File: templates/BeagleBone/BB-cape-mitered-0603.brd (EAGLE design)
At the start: 86.4 x 54.6 mm, 14 parts, among them IC8 EEPROM-I2CSMD

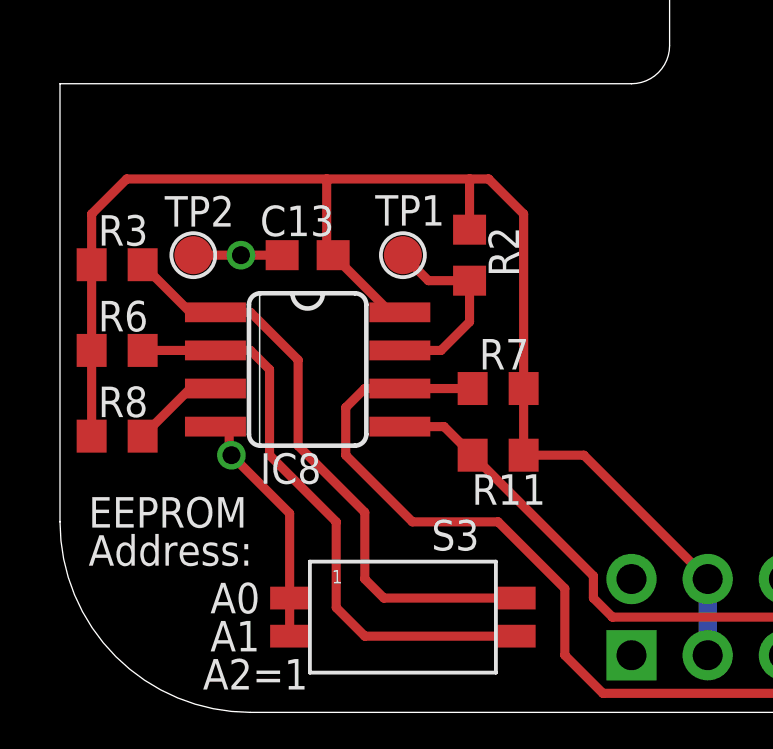
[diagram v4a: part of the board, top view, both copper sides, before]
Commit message: renumbered components on templates
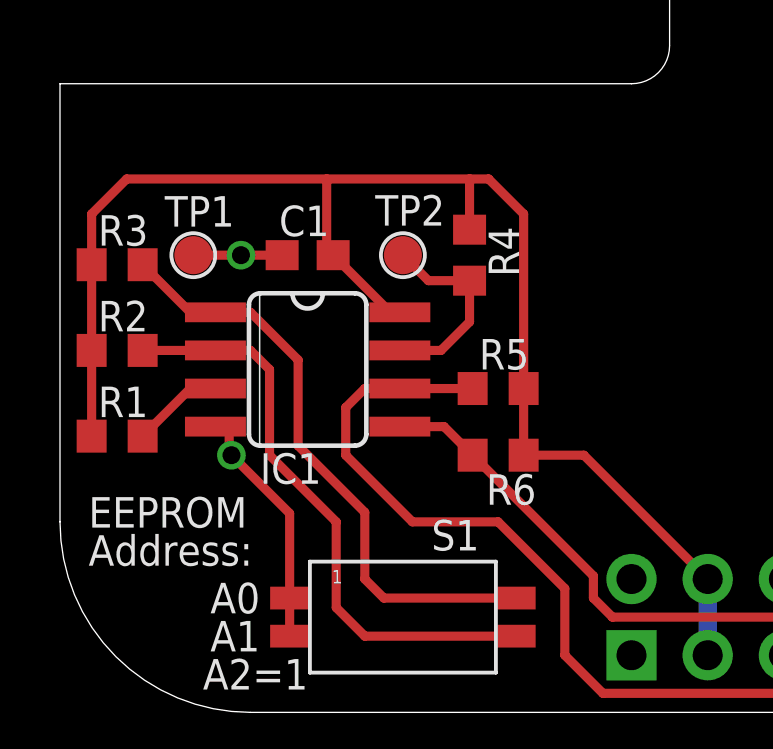
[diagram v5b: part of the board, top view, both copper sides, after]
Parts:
- removed R11: 5.6k, rcl:R0603
- added R4: 5.6k, rcl:R0603
- moved R6 13.2 mm to (14.6, 8.57), turned to 0 degrees
- moved R2 12.2 mm to (1.91, 12.1), turned to 180 degrees
- moved TP1 6.98 mm to (4.45, 15.2)
- moved TP2 6.98 mm to (11.4, 15.2)
- renumbered C13 to C1, IC8 to IC1, R7 to R5, R8 to R1, S3 to S1
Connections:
- net 3.3V: now also R4.2; no longer R11.2
- net GND: now also TP1.P$1; no longer TP2.P$1
- net I2C2_SDA: now also R6.1; no longer R11.1
- net N$14: now also R2.1; no longer R6.1
- net WP: now also R4.1, TP2.P$1; no longer R2.1, TP1.P$1
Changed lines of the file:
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@@
 <layer number="220" name="220bmp" color="21" fill="1" visible="no" active="no"/>
 <layer number="221" name="221bmp" color="22" fill="1" visible="no" active="no"/>
-<layer number="222" name="222bmp" color="23" fill="1" visible="no" active="no"/>
 <layer number="223" name="223bmp" color="24" fill="1" visible="no" active="no"/>
 <layer number="224" name="224bmp" color="25" fill="1" visible="no" active="no"/>
@@
 </autorouter>
 <elements>
-<element name="IC8" library="logic-supply" package="SO08" value="EEPROM-I2CSMD" x="8.255" y="11.43" smashed="yes" rot="R270">
+<element name="IC1" library="logic-supply" package="SO08" value="EEPROM-I2CSMD" x="8.255" y="11.43" smashed="yes" rot="R270">
 <attribute name="VALUE" x="7.62" y="12.7" size="0.4064" layer="27" rot="R270"/>
 <attribute name="NAME" x="6.6675" y="7.62" size="1.016" layer="25" font="vector"/>
@@
 </element>
 <element name="U$4" library="logic-supply" package="LOGO-LGX-LARGE" value="LOGO-LGX_LARGE" x="41.5925" y="31.75" smashed="yes"/>
-<element name="R7" library="rcl" package="R0603" value="5.6k" x="14.605" y="10.795" smashed="yes">
+<element name="R5" library="rcl" package="R0603" value="5.6k" x="14.605" y="10.795" smashed="yes">
 <attribute name="NAME" x="13.97" y="11.43" size="1.016" layer="25" font="vector"/>
 <attribute name="VALUE" x="13.97" y="8.89" size="1.27" layer="27"/>
 <attribute name="PARTNO" value="RC0603FR-074K7L" x="14.605" y="10.795" size="1.778" layer="27" display="off"/>
 </element>
-<element name="R11" library="rcl" package="R0603" value="5.6k" x="14.605" y="8.5725" smashed="yes">
-<attribute name="NAME" x="16.1925" y="7.9375" size="1.016" layer="25" font="vector" rot="R180"/>
+<element name="R6" library="rcl" package="R0603" value="5.6k" x="14.605" y="8.5725" smashed="yes">
+<attribute name="NAME" x="15.875" y="7.9375" size="1.016" layer="25" font="vector" rot="R180"/>
 <attribute name="VALUE" x="13.97" y="6.6675" size="1.27" layer="27"/>
 <attribute name="PARTNO" value="RC0603FR-074K7L" x="14.605" y="8.5725" size="1.778" layer="27" display="off"/>
 </element>
-<element name="R2" library="rcl" package="R0603" value="5.6k" x="13.6525" y="15.24" smashed="yes" rot="R90">
+<element name="R4" library="rcl" package="R0603" value="5.6k" x="13.6525" y="15.24" smashed="yes" rot="R90">
 <attribute name="NAME" x="14.2875" y="16.1925" size="1.016" layer="25" font="vector" rot="R270"/>
 <attribute name="VALUE" x="15.5575" y="14.605" size="1.27" layer="27" rot="R90"/>
 <attribute name="PARTNO" value="RC0603FR-074K7L" x="13.6525" y="15.24" size="1.778" layer="27" rot="R90" display="off"/>
 </element>
-<element name="TP1" library="logic-supply" package="TEST_POINT" value="TEST_POINT" x="11.43" y="15.24" smashed="yes">
+<element name="TP2" library="logic-supply" package="TEST_POINT" value="TEST_POINT" x="11.43" y="15.24" smashed="yes">
 <attribute name="NAME" x="10.50925" y="16.22425" size="1.016" layer="25" font="vector"/>
 <attribute name="VALUE" x="12.573" y="14.605" size="0.4064" layer="27" ratio="10"/>
@@
 <attribute name="PARTNO" value="RC0603FR-074K7L" x="1.905" y="14.9225" size="1.778" layer="27" rot="R180" display="off"/>
 </element>
-<element name="R6" library="rcl" package="R0603" value="5.6k" x="1.905" y="12.065" smashed="yes" rot="R180">
+<element name="R2" library="rcl" package="R0603" value="5.6k" x="1.905" y="12.065" smashed="yes" rot="R180">
 <attribute name="NAME" x="1.27" y="12.7" size="1.016" layer="25" font="vector"/>
 <attribute name="VALUE" x="2.54" y="13.97" size="1.27" layer="27" rot="R180"/>
 <attribute name="PARTNO" value="RC0603FR-074K7L" x="1.905" y="12.065" size="1.778" layer="27" rot="R180" display="off"/>
 </element>
-<element name="R8" library="rcl" package="R0603" value="5.6k" x="1.905" y="9.2075" smashed="yes" rot="R180">
+<element name="R1" library="rcl" package="R0603" value="5.6k" x="1.905" y="9.2075" smashed="yes" rot="R180">
 <attribute name="NAME" x="1.27" y="9.8425" size="1.016" layer="25" font="vector"/>
 <attribute name="VALUE" x="2.54" y="11.1125" size="1.27" layer="27" rot="R180"/>
 <attribute name="PARTNO" value="RC0603FR-074K7L" x="1.905" y="9.2075" size="1.778" layer="27" rot="R180" display="off"/>
 </element>
-<element name="C13" library="rcl" package="C0603" value="0.1uF" x="8.255" y="15.24" smashed="yes" rot="R180">
-<attribute name="NAME" x="6.6675" y="15.875" size="1.016" layer="25" font="vector"/>
+<element name="C1" library="rcl" package="C0603" value="0.1uF" x="8.255" y="15.24" smashed="yes" rot="R180">
+<attribute name="NAME" x="7.3025" y="15.875" size="1.016" layer="25" font="vector"/>
 <attribute name="VALUE" x="8.89" y="17.145" size="1.27" layer="27" rot="R180"/>
 <attribute name="PARTNO" value="C1608X7R1E104K080AA" x="8.255" y="15.24" size="1.778" layer="27" rot="R180" display="off"/>
 </element>
-<element name="S3" library="logic-supply" package="DIPSWITCH-2P-SMD-1.27" value="SW_DIP-2P" x="11.43" y="3.175" smashed="yes">
+<element name="S1" library="logic-supply" package="DIPSWITCH-2P-SMD-1.27" value="SW_DIP-2P" x="11.43" y="3.175" smashed="yes">
 <attribute name="NAME" x="12.3825" y="5.3975" size="1.016" layer="25" font="vector"/>
 <attribute name="VALUE" x="8.89" y="-0.635" size="1.27" layer="27"/>
@@
 <element name="BB1" library="logic-supply" package="BB_CAPE_TOP" value="BBH2" x="0" y="0" rot="MR90"/>
 <element name="U$7" library="logic-supply" package="OSHW-LOGO-M" value="OSHW-LOGOM" x="63.8175" y="31.75"/>
-<element name="TP2" library="logic-supply" package="TEST_POINT" value="TEST_POINT" x="4.445" y="15.24" smashed="yes">
+<element name="TP1" library="logic-supply" package="TEST_POINT" value="TEST_POINT" x="4.445" y="15.24" smashed="yes">
 <attribute name="BOM" value="EXCLUDE" x="4.445" y="15.24" size="1.778" layer="27" display="off"/>
 <attribute name="DATABASE" value="./../BOM/logic-supply-db.txt" x="4.445" y="15.24" size="1.778" layer="27" display="off"/>
@@
 <signals>
 <signal name="3.3V">
-<contactref element="R7" pad="2"/>
-<contactref element="R11" pad="2"/>
+<contactref element="R5" pad="2"/>
+<contactref element="R6" pad="2"/>
+<contactref element="R4" pad="2"/>
+<contactref element="IC1" pad="8"/>
+<contactref element="R3" pad="2"/>
 <contactref element="R2" pad="2"/>
-<contactref element="IC8" pad="8"/>
-<contactref element="R3" pad="2"/>
-<contactref element="R6" pad="2"/>
-<contactref element="R8" pad="2"/>
-<contactref element="C13" pad="1"/>
+<contactref element="R1" pad="2"/>
+<contactref element="C1" pad="1"/>
 <wire x1="1.055" y1="9.2075" x2="1.055" y2="12.065" width="0.3048" layer="1"/>
 <wire x1="1.055" y1="12.065" x2="1.055" y2="14.9225" width="0.3048" layer="1"/>
@@
 </signal>
 <signal name="GND">
-<contactref element="C13" pad="2"/>
-<contactref element="S3" pad="1A"/>
-<contactref element="S3" pad="2A"/>
-<contactref element="IC8" pad="4"/>
+<contactref element="C1" pad="2"/>
+<contactref element="S1" pad="1A"/>
+<contactref element="S1" pad="2A"/>
+<contactref element="IC1" pad="4"/>
 <wire x1="7.655" y1="2.54" x2="7.655" y2="3.81" width="0.3048" layer="1"/>
 <wire x1="5.1816" y1="9.525" x2="5.6388" y2="9.4488" width="0.3048" layer="1"/>
@@
 <contactref element="BB1" pad="P9.44"/>
 <contactref element="BB1" pad="P9.46"/>
-<contactref element="TP2" pad="P$1"/>
+<contactref element="TP1" pad="P$1"/>
 <wire x1="6.0325" y1="15.24" x2="4.445" y2="15.24" width="0.3048" layer="1"/>
 <wire x1="7.655" y1="3.81" x2="7.655" y2="6.6325" width="0.3048" layer="1"/>
@@
 </signal>
 <signal name="I2C2_SDA">
-<contactref element="IC8" pad="5"/>
-<contactref element="R11" pad="1"/>
+<contactref element="IC1" pad="5"/>
+<contactref element="R6" pad="1"/>
 <wire x1="11.3284" y1="9.525" x2="12.8025" y2="9.525" width="0.3048" layer="1"/>
 <wire x1="12.8025" y1="9.525" x2="13.755" y2="8.5725" width="0.3048" layer="1"/>
@@
 </signal>
 <signal name="I2C2_SCL">
-<contactref element="IC8" pad="6"/>
-<contactref element="R7" pad="1"/>
+<contactref element="IC1" pad="6"/>
+<contactref element="R5" pad="1"/>
 <wire x1="13.755" y1="10.795" x2="11.3284" y2="10.795" width="0.3048" layer="1"/>
 <wire x1="41.91" y1="1.5875" x2="40.9575" y2="0.635" width="0.3048" layer="1"/>
@@
 </signal>
 <signal name="WP">
-<contactref element="IC8" pad="7"/>
-<contactref element="TP1" pad="P$1"/>
+<contactref element="IC1" pad="7"/>
+<contactref element="TP2" pad="P$1"/>
 <wire x1="13.6525" y1="13.0175" x2="12.7" y2="12.065" width="0.3048" layer="1"/>
 <wire x1="12.7" y1="12.065" x2="11.3284" y2="12.065" width="0.3048" layer="1"/>
-<contactref element="R2" pad="1"/>
+<contactref element="R4" pad="1"/>
 <wire x1="13.6525" y1="14.39" x2="13.6525" y2="13.0175" width="0.3048" layer="1"/>
 <wire x1="13.6525" y1="14.39" x2="12.28" y2="14.39" width="0.3048" layer="1"/>
@@
 </signal>
 <signal name="N$13">
-<contactref element="IC8" pad="1"/>
+<contactref element="IC1" pad="1"/>
 <contactref element="R3" pad="1"/>
-<contactref element="S3" pad="1B"/>
+<contactref element="S1" pad="1B"/>
 <wire x1="5.1816" y1="13.335" x2="4.3425" y2="13.335" width="0.3048" layer="1"/>
 <wire x1="4.3425" y1="13.335" x2="2.755" y2="14.9225" width="0.3048" layer="1"/>
@@
 </signal>
 <signal name="N$14">
-<contactref element="IC8" pad="2"/>
-<contactref element="R6" pad="1"/>
-<contactref element="S3" pad="2B"/>
+<contactref element="IC1" pad="2"/>
+<contactref element="R2" pad="1"/>
+<contactref element="S1" pad="2B"/>
 <wire x1="5.1816" y1="12.065" x2="2.755" y2="12.065" width="0.3048" layer="1"/>
 <wire x1="15.205" y1="2.54" x2="10.16" y2="2.54" width="0.3048" layer="1"/>
@@
 </signal>
 <signal name="N$15">
-<contactref element="IC8" pad="3"/>
-<contactref element="R8" pad="1"/>
+<contactref element="IC1" pad="3"/>
+<contactref element="R1" pad="1"/>
 <wire x1="5.1816" y1="10.795" x2="4.3425" y2="10.795" width="0.3048" layer="1"/>
 <wire x1="4.3425" y1="10.795" x2="2.755" y2="9.2075" width="0.3048" layer="1"/>

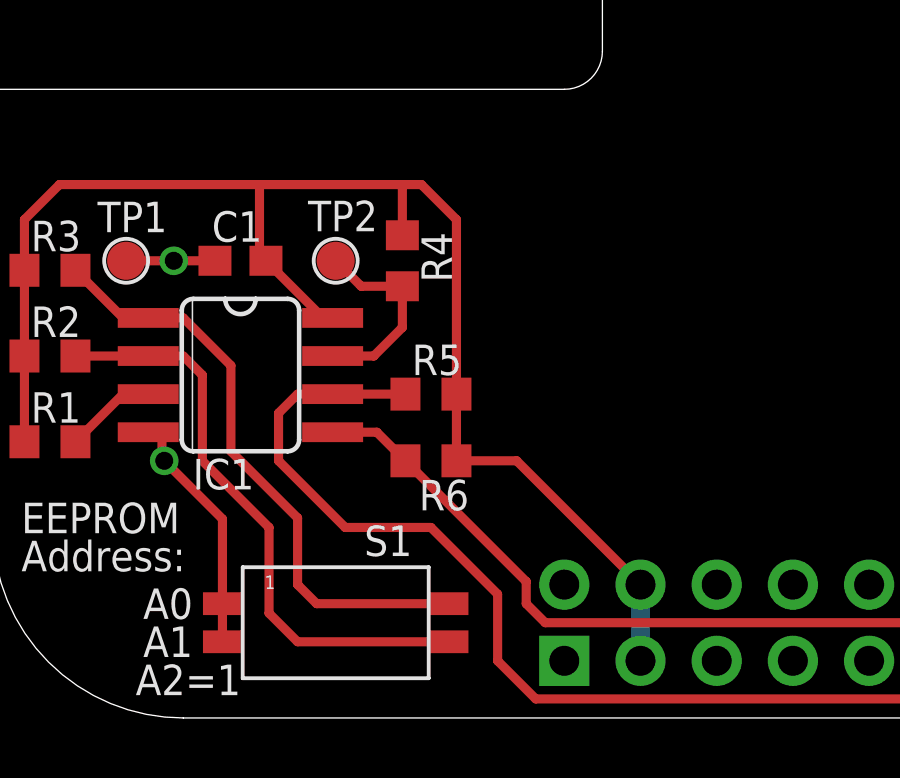
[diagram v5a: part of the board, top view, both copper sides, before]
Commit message: moved R4 (symmetry is nice!)
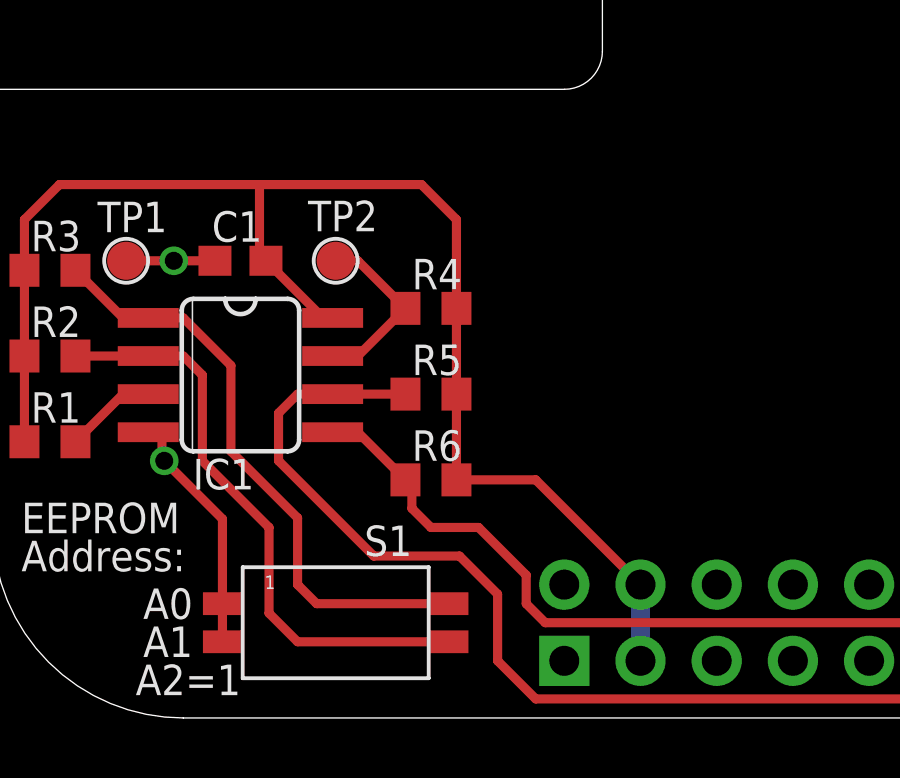
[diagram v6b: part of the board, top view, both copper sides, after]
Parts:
- moved R4 1.85 mm to (14.6, 13.7), turned to 0 degrees
- moved R6 0.63 mm to (14.6, 7.94)
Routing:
- net 3.3V: track 48.9 -> 47.5 mm
- net WP: track 6.67 -> 6.07 mm
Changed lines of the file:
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@@
 <attribute name="PARTNO" value="RC0603FR-074K7L" x="14.605" y="10.795" size="1.778" layer="27" display="off"/>
 </element>
-<element name="R6" library="rcl" package="R0603" value="5.6k" x="14.605" y="8.5725" smashed="yes">
-<attribute name="NAME" x="15.875" y="7.9375" size="1.016" layer="25" font="vector" rot="R180"/>
-<attribute name="VALUE" x="13.97" y="6.6675" size="1.27" layer="27"/>
-<attribute name="PARTNO" value="RC0603FR-074K7L" x="14.605" y="8.5725" size="1.778" layer="27" display="off"/>
+<element name="R6" library="rcl" package="R0603" value="5.6k" x="14.605" y="7.9375" smashed="yes">
+<attribute name="NAME" x="13.97" y="8.5725" size="1.016" layer="25" font="vector"/>
+<attribute name="VALUE" x="13.97" y="6.0325" size="1.27" layer="27"/>
+<attribute name="PARTNO" value="RC0603FR-074K7L" x="14.605" y="7.9375" size="1.778" layer="27" display="off"/>
 </element>
-<element name="R4" library="rcl" package="R0603" value="5.6k" x="13.6525" y="15.24" smashed="yes" rot="R90">
-<attribute name="NAME" x="14.2875" y="16.1925" size="1.016" layer="25" font="vector" rot="R270"/>
-<attribute name="VALUE" x="15.5575" y="14.605" size="1.27" layer="27" rot="R90"/>
-<attribute name="PARTNO" value="RC0603FR-074K7L" x="13.6525" y="15.24" size="1.778" layer="27" rot="R90" display="off"/>
+<element name="R4" library="rcl" package="R0603" value="5.6k" x="14.605" y="13.6525" smashed="yes">
+<attribute name="NAME" x="13.97" y="14.2875" size="1.016" layer="25" font="vector"/>
+<attribute name="VALUE" x="13.97" y="11.7475" size="1.27" layer="27"/>
+<attribute name="PARTNO" value="RC0603FR-074K7L" x="14.605" y="13.6525" size="1.778" layer="27" display="off"/>
 </element>
 <element name="TP2" library="logic-supply" package="TEST_POINT" value="TEST_POINT" x="11.43" y="15.24" smashed="yes">
@@
 <wire x1="1.055" y1="12.065" x2="1.055" y2="14.9225" width="0.3048" layer="1"/>
 <wire x1="11.5325" y1="13.3613" x2="11.3284" y2="13.335" width="0.3048" layer="1"/>
-<wire x1="15.455" y1="8.5725" x2="15.455" y2="10.795" width="0.3048" layer="1"/>
+<wire x1="15.455" y1="7.9375" x2="15.455" y2="10.795" width="0.3048" layer="1"/>
 <contactref element="BB1" pad="P9.3"/>
 <contactref element="BB1" pad="P9.4"/>
@@
 <wire x1="1.055" y1="16.6125" x2="2.2225" y2="17.78" width="0.3048" layer="1"/>
 <wire x1="2.2225" y1="17.78" x2="8.89" y2="17.78" width="0.3048" layer="1"/>
-<wire x1="8.89" y1="17.78" x2="13.6525" y2="17.78" width="0.3048" layer="1"/>
-<wire x1="13.6525" y1="17.78" x2="14.2875" y2="17.78" width="0.3048" layer="1"/>
+<wire x1="8.89" y1="17.78" x2="14.2875" y2="17.78" width="0.3048" layer="1"/>
 <wire x1="9.105" y1="15.24" x2="8.89" y2="15.24" width="0.3048" layer="1"/>
 <wire x1="8.89" y1="15.24" x2="8.89" y2="17.78" width="0.3048" layer="1"/>
 <wire x1="11.3284" y1="13.335" x2="11.01" y2="13.335" width="0.3048" layer="1"/>
 <wire x1="11.01" y1="13.335" x2="9.105" y2="15.24" width="0.3048" layer="1"/>
-<wire x1="21.59" y1="4.445" x2="17.4625" y2="8.5725" width="0.3048" layer="1"/>
-<wire x1="17.4625" y1="8.5725" x2="15.455" y2="8.5725" width="0.3048" layer="1"/>
-<wire x1="15.455" y1="10.795" x2="15.455" y2="16.6125" width="0.3048" layer="1"/>
+<wire x1="15.455" y1="10.795" x2="15.455" y2="13.335" width="0.3048" layer="1"/>
+<wire x1="15.455" y1="13.6525" x2="15.455" y2="16.6125" width="0.3048" layer="1"/>
 <wire x1="15.455" y1="16.6125" x2="14.2875" y2="17.78" width="0.3048" layer="1"/>
-<wire x1="13.6525" y1="16.09" x2="13.6525" y2="17.78" width="0.3048" layer="1"/>
+<wire x1="15.455" y1="7.9375" x2="18.0975" y2="7.9375" width="0.3048" layer="1"/>
+<wire x1="18.0975" y1="7.9375" x2="21.59" y2="4.445" width="0.3048" layer="1"/>
+<wire x1="15.455" y1="13.6525" x2="15.455" y2="13.335" width="0.3048" layer="1"/>
 </signal>
 <signal name="GND">
@@
 <contactref element="IC1" pad="5"/>
 <contactref element="R6" pad="1"/>
-<wire x1="11.3284" y1="9.525" x2="12.8025" y2="9.525" width="0.3048" layer="1"/>
-<wire x1="12.8025" y1="9.525" x2="13.755" y2="8.5725" width="0.3048" layer="1"/>
 <wire x1="41.91" y1="4.1275" x2="40.9575" y2="3.175" width="0.3048" layer="1"/>
 <wire x1="40.9575" y1="3.175" x2="18.415" y2="3.175" width="0.3048" layer="1"/>
-<wire x1="13.6525" y1="8.7875" x2="13.755" y2="8.5725" width="0.3048" layer="1"/>
 <contactref element="BB1" pad="P9.20"/>
 <wire x1="41.91" y1="4.1275" x2="41.91" y2="4.445" width="0.3048" layer="1"/>
 <wire x1="18.415" y1="3.175" x2="17.78" y2="3.81" width="0.3048" layer="1"/>
-<wire x1="17.78" y1="3.81" x2="17.78" y2="4.5475" width="0.3048" layer="1"/>
-<wire x1="17.78" y1="4.5475" x2="13.755" y2="8.5725" width="0.3048" layer="1"/>
+<wire x1="17.78" y1="3.81" x2="17.78" y2="4.7625" width="0.3048" layer="1"/>
+<wire x1="17.78" y1="4.7625" x2="16.1925" y2="6.35" width="0.3048" layer="1"/>
+<wire x1="16.1925" y1="6.35" x2="14.605" y2="6.35" width="0.3048" layer="1"/>
+<wire x1="14.605" y1="6.35" x2="13.97" y2="6.985" width="0.3048" layer="1"/>
+<wire x1="13.97" y1="6.985" x2="13.97" y2="7.7225" width="0.3048" layer="1"/>
+<wire x1="13.97" y1="7.7225" x2="13.755" y2="7.9375" width="0.3048" layer="1"/>
+<wire x1="11.3284" y1="9.525" x2="12.1675" y2="9.525" width="0.3048" layer="1"/>
+<wire x1="12.1675" y1="9.525" x2="13.755" y2="7.9375" width="0.3048" layer="1"/>
 </signal>
 <signal name="I2C2_SCL">
@@
 <wire x1="18.0975" y1="0.635" x2="16.8275" y2="1.905" width="0.3048" layer="1"/>
 <wire x1="16.8275" y1="1.905" x2="16.8275" y2="4.1275" width="0.3048" layer="1"/>
-<wire x1="16.8275" y1="4.1275" x2="14.605" y2="6.35" width="0.3048" layer="1"/>
-<wire x1="14.605" y1="6.35" x2="11.7475" y2="6.35" width="0.3048" layer="1"/>
-<wire x1="11.7475" y1="6.35" x2="9.525" y2="8.5725" width="0.3048" layer="1"/>
+<wire x1="16.8275" y1="4.1275" x2="15.5575" y2="5.3975" width="0.3048" layer="1"/>
+<wire x1="15.5575" y1="5.3975" x2="12.7" y2="5.3975" width="0.3048" layer="1"/>
+<wire x1="12.7" y1="5.3975" x2="9.525" y2="8.5725" width="0.3048" layer="1"/>
 <wire x1="9.525" y1="8.5725" x2="9.525" y2="10.16" width="0.3048" layer="1"/>
 <wire x1="9.525" y1="10.16" x2="10.16" y2="10.795" width="0.3048" layer="1"/>
@@
 <contactref element="IC1" pad="7"/>
 <contactref element="TP2" pad="P$1"/>
-<wire x1="13.6525" y1="13.0175" x2="12.7" y2="12.065" width="0.3048" layer="1"/>
-<wire x1="12.7" y1="12.065" x2="11.3284" y2="12.065" width="0.3048" layer="1"/>
 <contactref element="R4" pad="1"/>
-<wire x1="13.6525" y1="14.39" x2="13.6525" y2="13.0175" width="0.3048" layer="1"/>
-<wire x1="13.6525" y1="14.39" x2="12.28" y2="14.39" width="0.3048" layer="1"/>
-<wire x1="12.28" y1="14.39" x2="11.43" y2="15.24" width="0.3048" layer="1"/>
+<wire x1="11.43" y1="15.24" x2="12.1675" y2="15.24" width="0.3048" layer="1"/>
+<wire x1="12.1675" y1="15.24" x2="13.755" y2="13.6525" width="0.3048" layer="1"/>
+<wire x1="11.3284" y1="12.065" x2="12.1675" y2="12.065" width="0.3048" layer="1"/>
+<wire x1="12.1675" y1="12.065" x2="13.755" y2="13.6525" width="0.3048" layer="1"/>
 </signal>
 <signal name="N$13">
